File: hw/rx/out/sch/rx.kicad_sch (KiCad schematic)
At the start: 0 parts

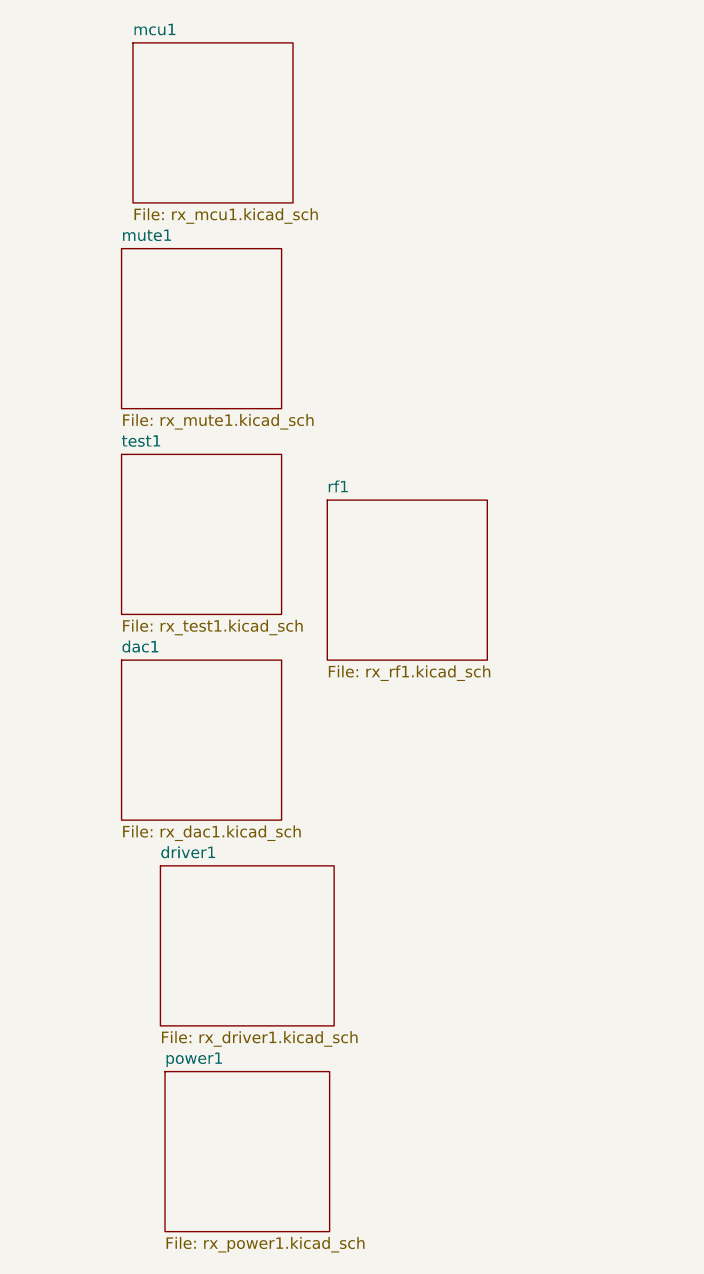
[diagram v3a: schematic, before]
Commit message: hw/rx + hw/pack: #116 review fixes: netclass pour clearances (no 0.09 mm override), keyed J1 with no hole at 14, solid RF grounds, K1 pin-1/CPL rotation, raw RF numbers (#34)
- M1: JLC copper-clearance rule removed from rx and pack .kicad_dru; boards refilled/regenerated; probe-rule tests
  assert >= 0.125 mm everywhere and >= 0.15 mm to Audio_I on the committed fill; outer-copper rule width-independent
- S1: openpack:PinHeader_2x13_P2.54mm_Key14 (pad 14 deleted, KEY silk), header XFCN PZ254V-12-26P (LCSC C22465887,
  pin 14 cut), main-board socket Samtec SSW-113-01-G-D-14 recorded in ADR-0014; test
- S2: zone_connect solid on J3-J5, U2, U1 GND pads; test
- S3: TQ2SA pin-1 dot + '+', CPL +270 for the relay (K1 at 180); pin-1 marker + CPL test for all polarized parts
- N1 raw RF Z0 (51.5 bare / ~49.3 masked), N3 C44 at U6, REVIEW follow-ups

Co-Authored-By: Claude Opus 5.5 <noreply@anthropic.com>
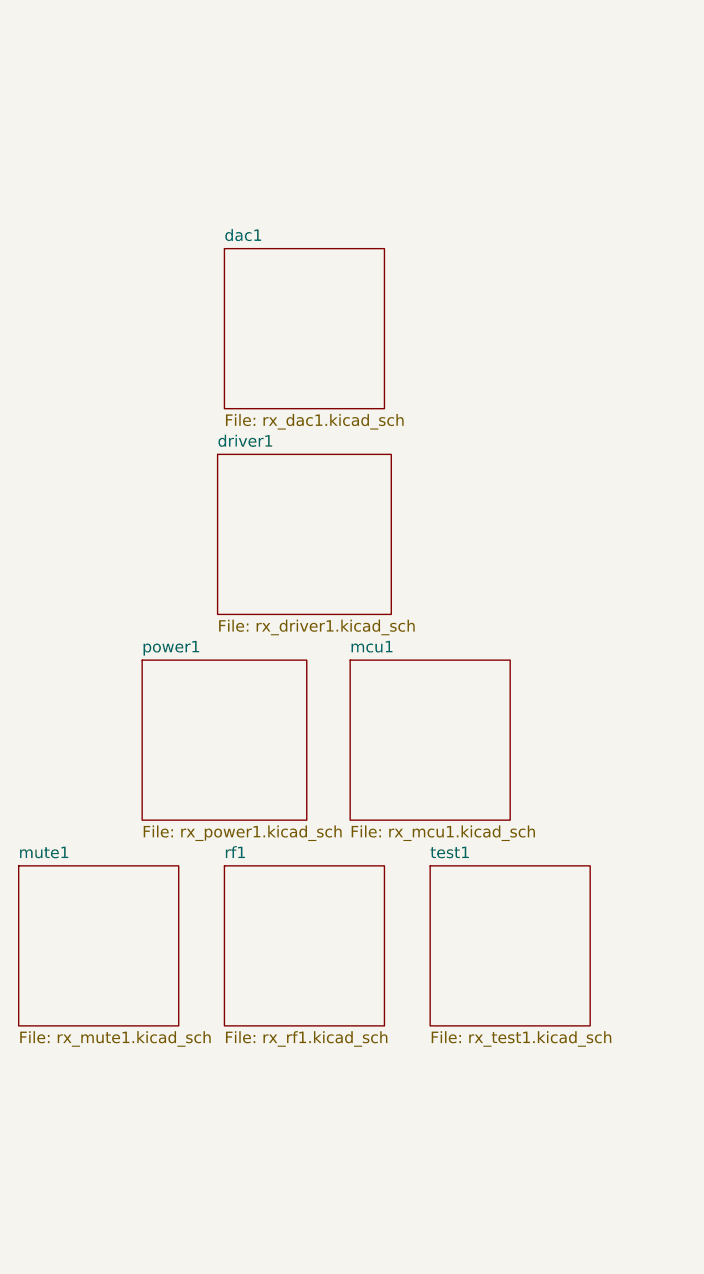
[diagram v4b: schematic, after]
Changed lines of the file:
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@@
     (comment 4 ""))
   (sheet
-    (at 133.1 153.67)
+    (at 130.56 107.95)
     (size 18.29 17.78)
     (exclude_from_sim no)
@@
       (color 0 0 0 0.0))
     (property "Sheetname" "power1"
-      (at 133.1 152.96 0)
+      (at 130.56 107.24 0)
       (effects
         (font
@@
         (justify left bottom)))
     (property "Sheetfile" "rx_power1.kicad_sch"
-      (at 133.1 172.03 0)
+      (at 130.56 126.31 0)
       (effects
         (font
@@
         (justify left top))))
   (sheet
-    (at 129.54 39.37)
+    (at 153.67 107.95)
     (size 17.78 17.78)
     (exclude_from_sim no)
@@
       (color 0 0 0 0.0))
     (property "Sheetname" "mcu1"
-      (at 129.54 38.66 0)
+      (at 153.67 107.24 0)
       (effects
         (font
@@
         (justify left bottom)))
     (property "Sheetfile" "rx_mcu1.kicad_sch"
-      (at 129.54 57.73 0)
+      (at 153.67 126.31 0)
       (effects
         (font
@@
         (justify left top))))
   (sheet
-    (at 151.13 90.17)
+    (at 139.7 130.81)
     (size 17.78 17.78)
     (exclude_from_sim no)
@@
       (color 0 0 0 0.0))
     (property "Sheetname" "rf1"
-      (at 151.13 89.46 0)
+      (at 139.7 130.1 0)
       (effects
         (font
@@
         (justify left bottom)))
     (property "Sheetfile" "rx_rf1.kicad_sch"
-      (at 151.13 108.53 0)
+      (at 139.7 149.17 0)
       (effects
         (font
@@
         (justify left top))))
   (sheet
-    (at 128.27 107.95)
+    (at 139.7 62.23)
     (size 17.78 17.78)
     (exclude_from_sim no)
@@
       (color 0 0 0 0.0))
     (property "Sheetname" "dac1"
-      (at 128.27 107.24 0)
+      (at 139.7 61.52 0)
       (effects
         (font
@@
         (justify left bottom)))
     (property "Sheetfile" "rx_dac1.kicad_sch"
-      (at 128.27 126.31 0)
+      (at 139.7 80.59 0)
       (effects
         (font
@@
         (justify left top))))
   (sheet
-    (at 132.59 130.81)
+    (at 138.94 85.09)
     (size 19.3 17.78)
     (exclude_from_sim no)
@@
       (color 0 0 0 0.0))
     (property "Sheetname" "driver1"
-      (at 132.59 130.1 0)
+      (at 138.94 84.38 0)
       (effects
         (font
@@
         (justify left bottom)))
     (property "Sheetfile" "rx_driver1.kicad_sch"
-      (at 132.59 149.17 0)
+      (at 138.94 103.45 0)
       (effects
         (font
@@
         (justify left top))))
   (sheet
-    (at 128.27 62.23)
+    (at 116.84 130.81)
     (size 17.78 17.78)
     (exclude_from_sim no)
@@
       (color 0 0 0 0.0))
     (property "Sheetname" "mute1"
-      (at 128.27 61.52 0)
+      (at 116.84 130.1 0)
       (effects
         (font
@@
         (justify left bottom)))
     (property "Sheetfile" "rx_mute1.kicad_sch"
-      (at 128.27 80.59 0)
+      (at 116.84 149.17 0)
       (effects
         (font
@@
         (justify left top))))
   (sheet
-    (at 128.27 85.09)
+    (at 162.56 130.81)
     (size 17.78 17.78)
     (exclude_from_sim no)
@@
       (color 0 0 0 0.0))
     (property "Sheetname" "test1"
-      (at 128.27 84.38 0)
+      (at 162.56 130.1 0)
       (effects
         (font
@@
         (justify left bottom)))
     (property "Sheetfile" "rx_test1.kicad_sch"
-      (at 128.27 103.45 0)
+      (at 162.56 149.17 0)
       (effects
         (font
